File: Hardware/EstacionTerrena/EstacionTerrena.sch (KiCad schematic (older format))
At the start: 5 parts, among them J1 5-1814832-1

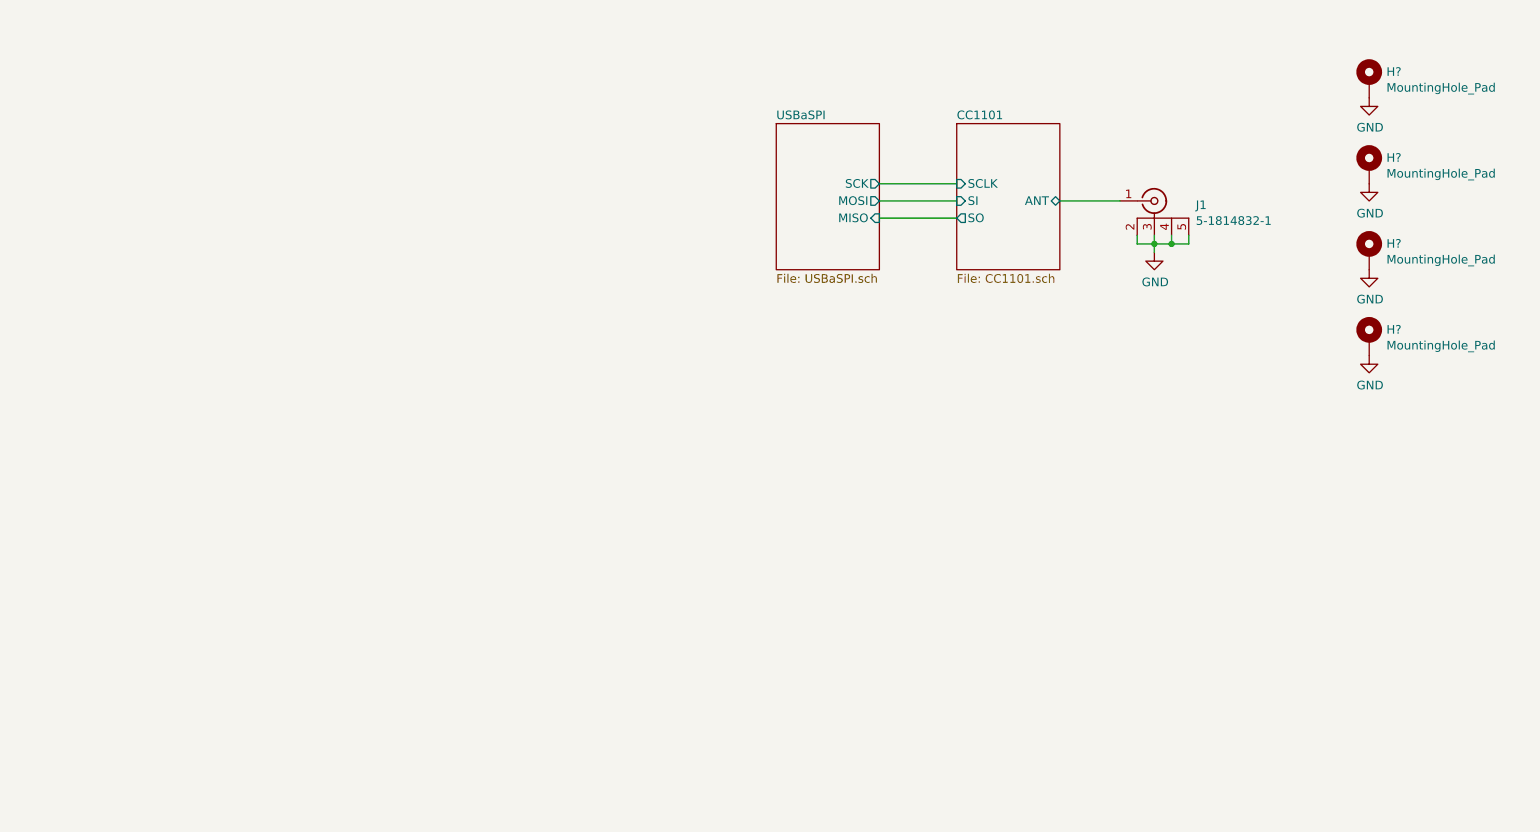
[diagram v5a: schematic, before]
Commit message: Agregado logo y cambio de posición de LEDs a PCB de estación terrena
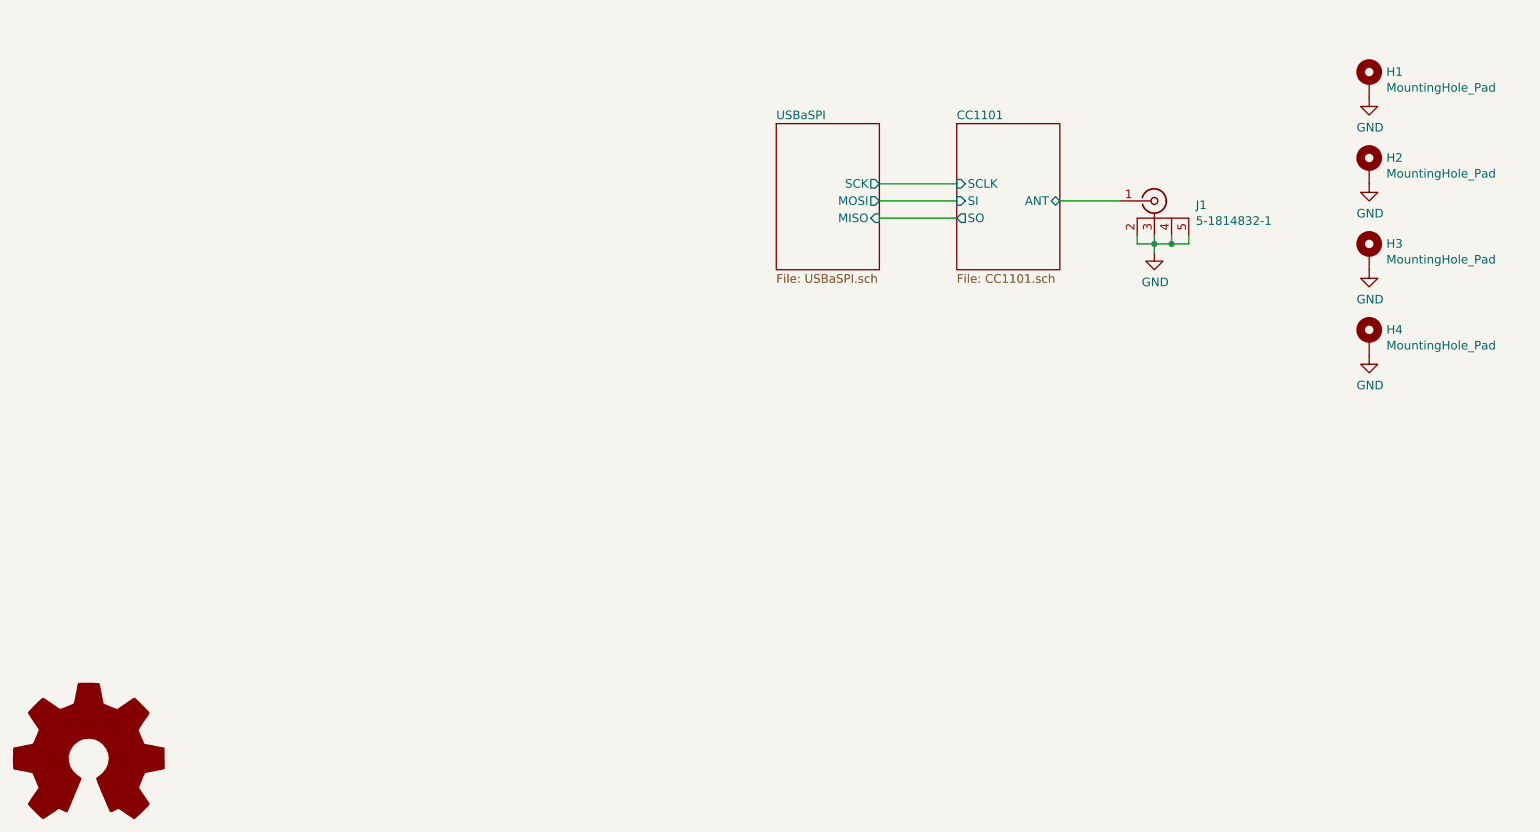
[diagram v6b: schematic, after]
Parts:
- gave numbers to parts that had none: 4
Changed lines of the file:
@@
 	7250 4350 7250 4300
 $Comp
-L Mechanical:MountingHole_Pad H?
+L Mechanical:MountingHole_Pad H1
 U 1 1 5BBFD953
 P 8500 3350
-F 0 "H?" H 8600 3401 50  0000 L CNN
+F 0 "H1" H 8600 3401 50  0000 L CNN
 F 1 "MountingHole_Pad" H 8600 3309 50  0000 L CNN
 F 2 "MountingHole:MountingHole_3.2mm_M3_Pad" H 8500 3350 50  0001 C CNN
@@
 $EndComp
 $Comp
-L Mechanical:MountingHole_Pad H?
+L Mechanical:MountingHole_Pad H2
 U 1 1 5BBFDA3A
 P 8500 3850
-F 0 "H?" H 8600 3901 50  0000 L CNN
+F 0 "H2" H 8600 3901 50  0000 L CNN
 F 1 "MountingHole_Pad" H 8600 3809 50  0000 L CNN
 F 2 "MountingHole:MountingHole_3.2mm_M3_Pad" H 8500 3850 50  0001 C CNN
@@
 $EndComp
 $Comp
-L Mechanical:MountingHole_Pad H?
+L Mechanical:MountingHole_Pad H3
 U 1 1 5BBFDA66
 P 8500 4350
-F 0 "H?" H 8600 4401 50  0000 L CNN
+F 0 "H3" H 8600 4401 50  0000 L CNN
 F 1 "MountingHole_Pad" H 8600 4309 50  0000 L CNN
 F 2 "MountingHole:MountingHole_3.2mm_M3_Pad" H 8500 4350 50  0001 C CNN
@@
 $EndComp
 $Comp
-L Mechanical:MountingHole_Pad H?
+L Mechanical:MountingHole_Pad H4
 U 1 1 5BBFDA96
 P 8500 4850
-F 0 "H?" H 8600 4901 50  0000 L CNN
+F 0 "H4" H 8600 4901 50  0000 L CNN
 F 1 "MountingHole_Pad" H 8600 4809 50  0000 L CNN
 F 2 "MountingHole:MountingHole_3.2mm_M3_Pad" H 8500 4850 50  0001 C CNN
@@
 $EndComp
 $Comp
-L power:GND #PWR?
+L power:GND #PWR0101
 U 1 1 5BBFDACC
 P 8500 3450
-F 0 "#PWR?" H 8500 3200 50  0001 C CNN
+F 0 "#PWR0101" H 8500 3200 50  0001 C CNN
 F 1 "GND" H 8505 3277 50  0000 C CNN
 F 2 "" H 8500 3450 50  0001 C CNN
@@
 $EndComp
 $Comp
-L power:GND #PWR?
+L power:GND #PWR0102
 U 1 1 5BBFDAE9
 P 8500 3950
-F 0 "#PWR?" H 8500 3700 50  0001 C CNN
+F 0 "#PWR0102" H 8500 3700 50  0001 C CNN
 F 1 "GND" H 8505 3777 50  0000 C CNN
 F 2 "" H 8500 3950 50  0001 C CNN
@@
 $EndComp
 $Comp
-L power:GND #PWR?
+L power:GND #PWR0103
 U 1 1 5BBFDB80
 P 8500 4450
-F 0 "#PWR?" H 8500 4200 50  0001 C CNN
+F 0 "#PWR0103" H 8500 4200 50  0001 C CNN
 F 1 "GND" H 8505 4277 50  0000 C CNN
 F 2 "" H 8500 4450 50  0001 C CNN
@@
 $EndComp
 $Comp
-L power:GND #PWR?
+L power:GND #PWR0104
 U 1 1 5BBFDB9D
 P 8500 4950
-F 0 "#PWR?" H 8500 4700 50  0001 C CNN
+F 0 "#PWR0104" H 8500 4700 50  0001 C CNN
 F 1 "GND" H 8505 4777 50  0000 C CNN
 F 2 "" H 8500 4950 50  0001 C CNN
@@
 	1    0    0    -1
 $EndComp
+$Comp
+L Graphic:Logo_Open_Hardware_Large #LOGO?
+U 1 1 5BBFDFCD
+P 1050 7300
+F 0 "#LOGO?" H 1050 7800 50  0001 C CNN
+F 1 "Logo_Open_Hardware_Large" H 1050 6900 50  0001 C CNN
+F 2 "Symbol:OSHW-Logo2_9.8x8mm_SilkScreen" H 1050 7300 50  0001 C CNN
+F 3 "~" H 1050 7300 50  0001 C CNN
+	1    1050 7300
+	1    0    0    -1
+$EndComp

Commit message: Agregado jumper para CS en estacion terrena
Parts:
- added J3: Conn_01x03, Connector_PinHeader_2.54mm:PinHeader_1x03_P2.54mm_Horizontal, symbol Connector_Generic:Conn_01x03
- added JP1: BOM_Jumper, AXTEC:Empty_Footprint, symbol AXTEC_IC:BOM_Jumper
- J1: footprint 5-1814832-1 -> SamacSys_Parts:5-1814832-1
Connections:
- net GND: now also J3.1 (Pin_1)
- new net CC1101/CS: J3.2 (Pin_2)
- new net USBaSPI/CS: J3.3 (Pin_3)
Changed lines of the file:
@@
 F3 "SCK" O R 5650 3950 50
 F4 "MISO" I R 5650 4150 50
+F5 "CS" O R 5650 4250 50
 $EndSheet
 $Sheet
@@
 F4 "SI" I L 6100 4050 50
 F5 "ANT" B R 6700 4050 50
+F6 "CS" I L 6100 4250 50
 $EndSheet
 Wire Wire Line
@@
 F 0 "J1" H 7491 4026 50  0000 L CNN
 F 1 "5-1814832-1" H 7491 3934 50  0000 L CNN
-F 2 "5-1814832-1" H 7650 4150 50  0001 L CNN
+F 2 "SamacSys_Parts:5-1814832-1" H 7650 4150 50  0001 L CNN
 F 3 "http://www.te.com/commerce/DocumentDelivery/DDEController?Action=srchrtrv&DocNm=1814832&DocType=Customer+Drawing&DocLang=English" H 7650 4050 50  0001 L CNN
 F 4 "SUBMINIATURE COAX" H 7650 3950 50  0001 L CNN "Description"
@@
 $EndComp
 $Comp
-L Graphic:Logo_Open_Hardware_Large #LOGO?
+L Graphic:Logo_Open_Hardware_Large #LOGO1
 U 1 1 5BBFDFCD
 P 1050 7300
-F 0 "#LOGO?" H 1050 7800 50  0001 C CNN
+F 0 "#LOGO1" H 1050 7800 50  0001 C CNN
 F 1 "Logo_Open_Hardware_Large" H 1050 6900 50  0001 C CNN
 F 2 "Symbol:OSHW-Logo2_9.8x8mm_SilkScreen" H 1050 7300 50  0001 C CNN
@@
 	1    0    0    -1
 $EndComp
+$Comp
+L Connector_Generic:Conn_01x03 J3
+U 1 1 5C00A33C
+P 5900 4900
+F 0 "J3" V 5773 5080 50  0000 L CNN
+F 1 "Conn_01x03" V 5864 5080 50  0000 L CNN
+F 2 "Connector_PinHeader_2.54mm:PinHeader_1x03_P2.54mm_Horizontal" H 5900 4900 50  0001 C CNN
+F 3 "~" H 5900 4900 50  0001 C CNN
+	1    5900 4900
+	0    1    1    0
+$EndComp
+Wire Wire Line
+	5650 4250 5800 4250
+Wire Wire Line
+	5800 4250 5800 4700
+Wire Wire Line
+	6100 4250 5900 4250
+Wire Wire Line
+	5900 4250 5900 4700
+$Comp
+L power:GND #PWR026
+U 1 1 5C00A55B
+P 6650 4800
+F 0 "#PWR026" H 6650 4550 50  0001 C CNN
+F 1 "GND" H 6655 4627 50  0000 C CNN
+F 2 "" H 6650 4800 50  0001 C CNN
+F 3 "" H 6650 4800 50  0001 C CNN
+	1    6650 4800
+	1    0    0    -1
+$EndComp
+Wire Wire Line
+	6000 4700 6000 4600
+Wire Wire Line
+	6000 4600 6650 4600
+Wire Wire Line
+	6650 4600 6650 4800
+$Comp
+L AXTEC_IC:BOM_Jumper JP1
+U 1 1 5C00354F
+P 5950 5200
+F 0 "JP1" H 6113 5273 50  0000 L CNN
+F 1 "BOM_Jumper" H 6113 5182 50  0000 L CNN
+F 2 "AXTEC:Empty_Footprint" H 5950 5300 50  0001 C CNN
+F 3 "" H 5950 5300 50  0001 C CNN
+F 4 "M7581-05" H 6113 5091 50  0000 L CNN "Manufacturer Part Number"
+	1    5950 5200
+	1    0    0    -1
+$EndComp

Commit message: Componentes 0402 para el CC1101 en estación terrena
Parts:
- J3: Manufacturer Part Number (none) -> 61300311121
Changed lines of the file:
@@
 F 2 "Connector_PinHeader_2.54mm:PinHeader_1x03_P2.54mm_Horizontal" H 5900 4900 50  0001 C CNN
 F 3 "~" H 5900 4900 50  0001 C CNN
+F 4 "61300311121" V 5900 4900 50  0001 C CNN "Manufacturer Part Number"
 	1    5900 4900
 	0    1    1    0
